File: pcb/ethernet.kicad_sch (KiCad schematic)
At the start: 46 parts, among them U9 W5500, Y1 25MHz

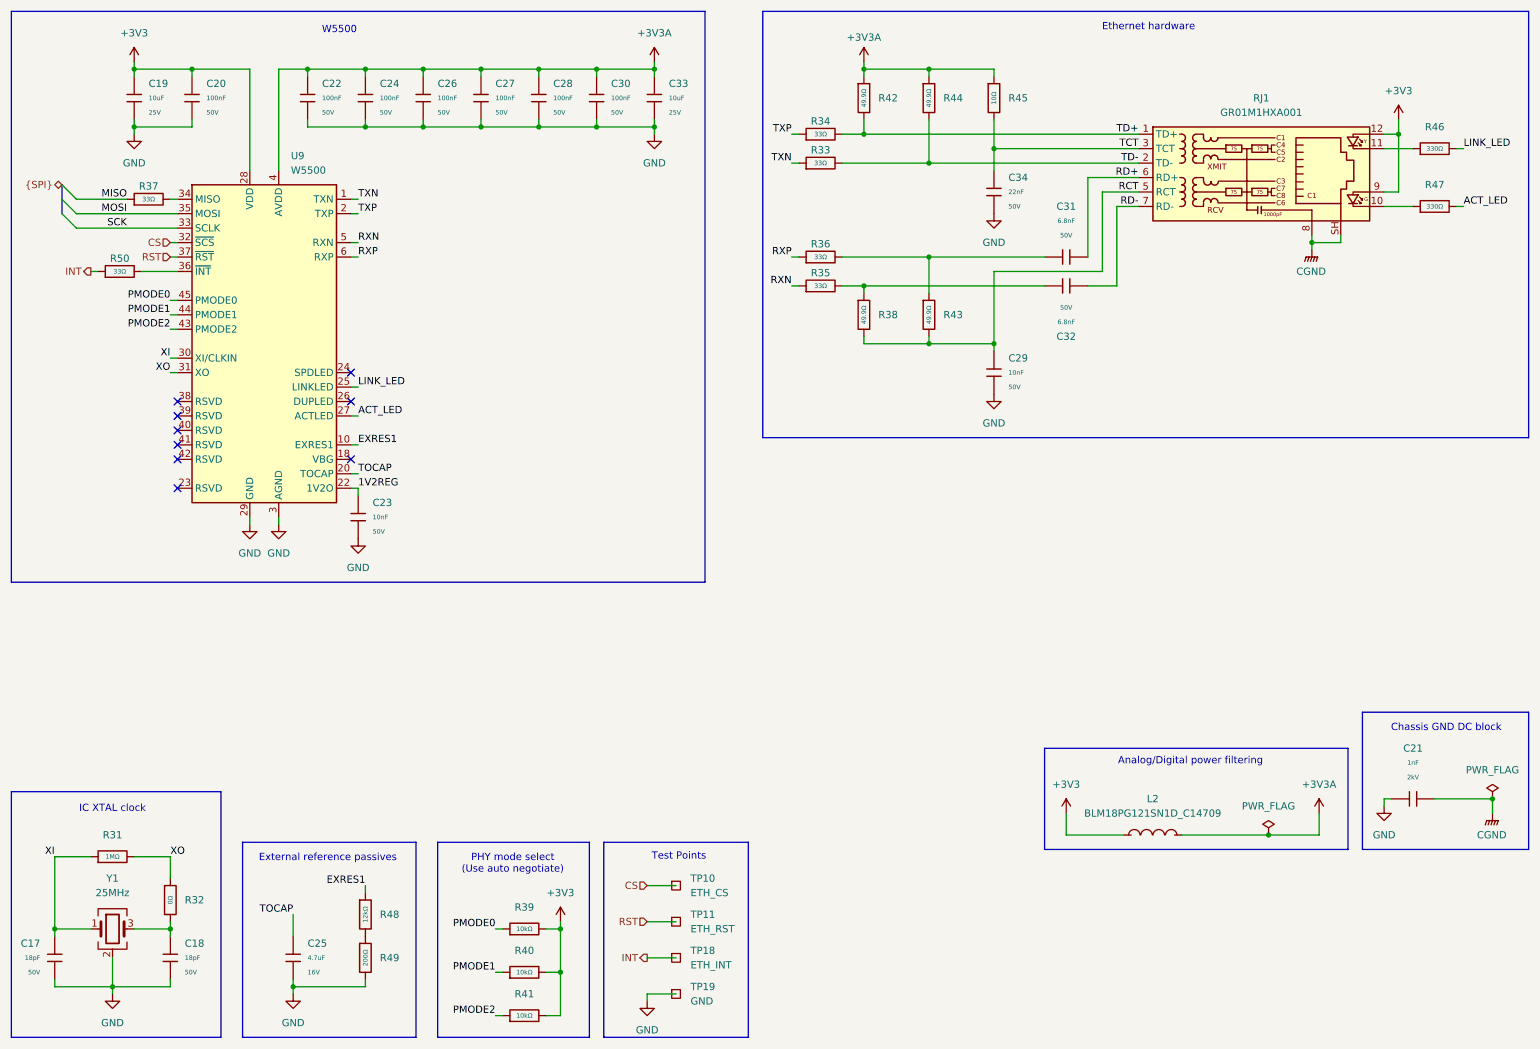
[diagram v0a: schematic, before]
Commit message: sch: rewire SPI to supply separate clock lines to flash and ethernet
The flash IC datasheet specifies that the SPI clock must not be toggled
while CS is high, which means we need to separate the ethernet and flash
clock lines.

I've GPIO3 on the ESP for the flash clock line, and plan to use the
internal peripheral MUX to switch it when talking with the IC.

I've also moved a bunch of test points and termination resistors in this
process.
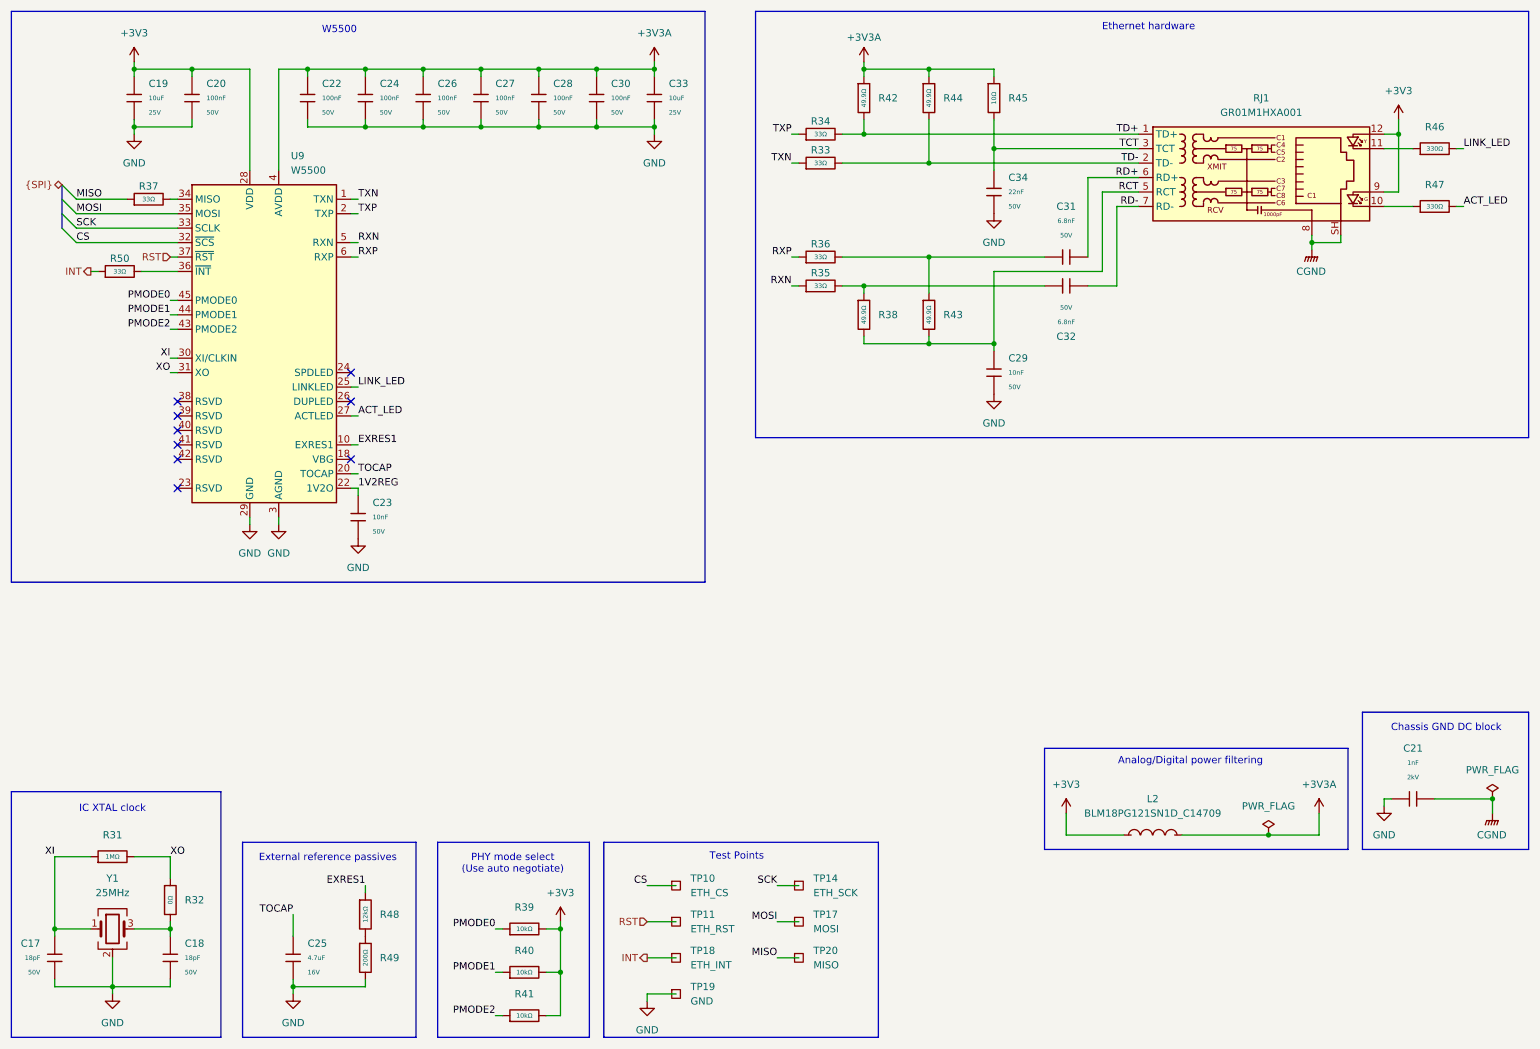
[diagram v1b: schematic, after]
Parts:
- added TP14: ETH_SCK, TestPoint:TestPoint_Pad_D1.0mm, symbol Connector:TestPoint_Square
- added TP17: MOSI, TestPoint:TestPoint_Pad_D1.0mm, symbol Connector:TestPoint_Square
- added TP20: MISO, TestPoint:TestPoint_Pad_D1.0mm, symbol Connector:TestPoint_Square
- TP10, TP11, TP18, TP19: now left out of the parts list
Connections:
- net MISO: now also TP20.1
- net MOSI: now also TP17.1
- net SCK: now also TP14.1

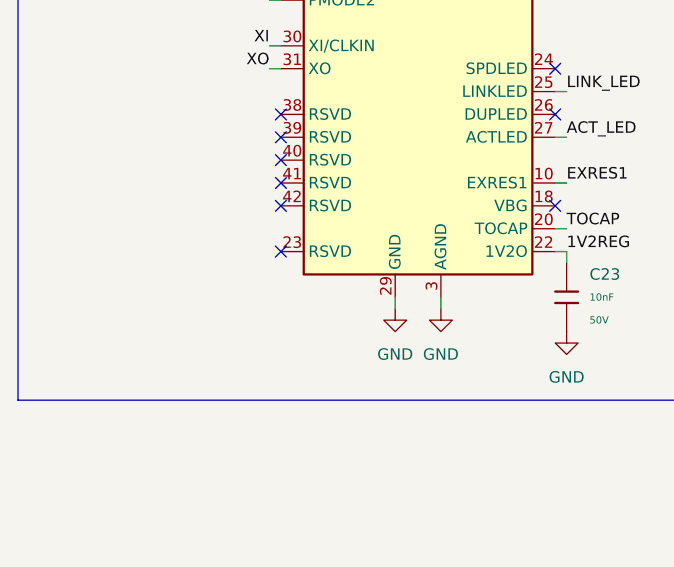
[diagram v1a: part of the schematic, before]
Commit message: sch: connect reserved W5500 pin 23 to ground
Pin 23 should be tied to ground according to the datasheet.
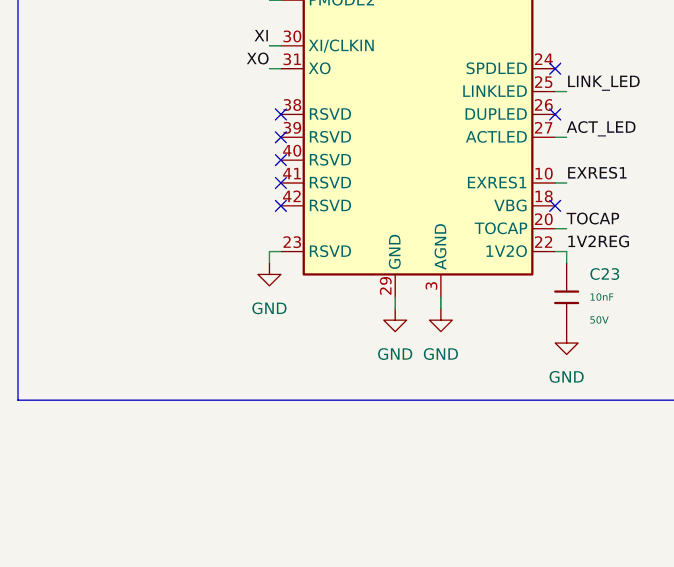
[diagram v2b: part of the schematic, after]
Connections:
- net GND: now also U9.23 (RSVD)
- no-connect marks 9 -> 8
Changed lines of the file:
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@@
 	)
 	(no_connect
-		(at 44.45 99.06)
-	)
-	(no_connect
 		(at 74.93 83.82)
 	)
@@
 	(wire
 		(pts
+			(xy 43.18 100.33) (xy 43.18 99.06)
+		)
+		(stroke
+			(width 0)
+			(type default)
+		)
+	)
+	(wire
+		(pts
 			(xy 176.53 25.4) (xy 187.96 25.4)
 		)
@@
 	(wire
 		(pts
+			(xy 43.18 99.06) (xy 44.45 99.06)
+		)
+		(stroke
+			(width 0)
+			(type default)
+		)
+	)
+	(wire
+		(pts
 			(xy 77.47 35.56) (xy 87.63 35.56)
 		)
@@
 					(unit 1)
 				)
+			)
+		)
+	)
+	(symbol
+		(lib_id "power:GND")
+		(at 43.18 100.33 0)
+		(mirror y)
+		(unit 1)
+		(body_style 1)
+		(exclude_from_sim no)
+		(in_bom yes)
+		(on_board yes)
+		(in_pos_files yes)
+		(dnp no)
+		(fields_autoplaced yes)
+		(property "Reference" "#PWR076"
+			(at 43.18 106.68 0)
+			(hide yes)
+			(show_name no)
+			(do_not_autoplace no)
+			(effects
+				(font
+					(size 1.27 1.27)
+				)
+			)
+		)
+		(property "Value" "GND"
+			(at 43.18 105.41 0)
+			(show_name no)
+			(do_not_autoplace no)
+			(effects
+				(font
+					(size 1.27 1.27)
+				)
+			)
+		)
+		(property "Footprint" ""
+			(at 43.18 100.33 0)
+			(hide yes)
+			(show_name no)
+			(do_not_autoplace no)
+			(effects
+				(font
+					(size 1.27 1.27)
+				)
+			)
+		)
+		(property "Datasheet" ""
+			(at 43.18 100.33 0)
+			(hide yes)
+			(show_name no)
+			(do_not_autoplace no)
+			(effects
+				(font
+					(size 1.27 1.27)
+				)
+			)
+		)
+		(property "Description" "Power symbol creates a global label with name \"GND\" , ground"
+			(at 43.18 100.33 0)
+			(hide yes)
+			(show_name no)
+			(do_not_autoplace no)
+			(effects
+				(font
+					(size 1.27 1.27)
+				)
+			)
+		)
+		(pin "1"
+		)
+		(instances
+			(project "EveningStar"
+				(path "/4c61f5a2-f8d4-462a-9bc3-d74437d30372/561d5dbe-6020-48c7-be42-1a6149a1119b"
+					(reference "#PWR076")
+					(unit 1)
+				)

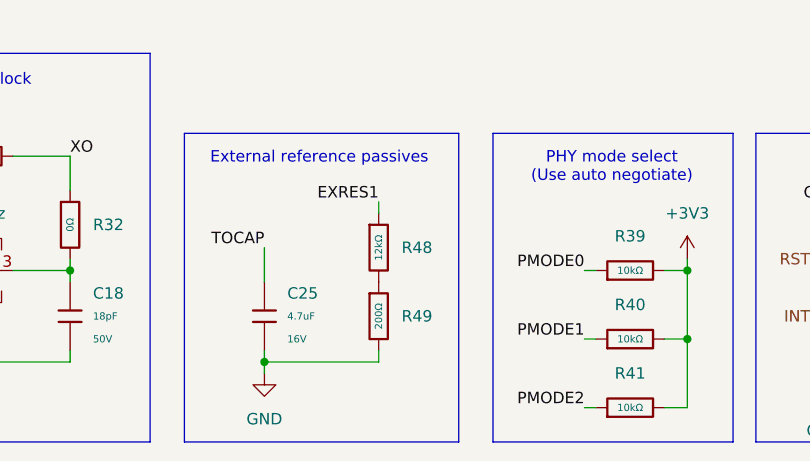
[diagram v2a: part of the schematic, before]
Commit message: sch: replace 12.2k w5500 exres with 12.4k
Datasheet specifies 12.4k resistor not 12.2k which was a mistake
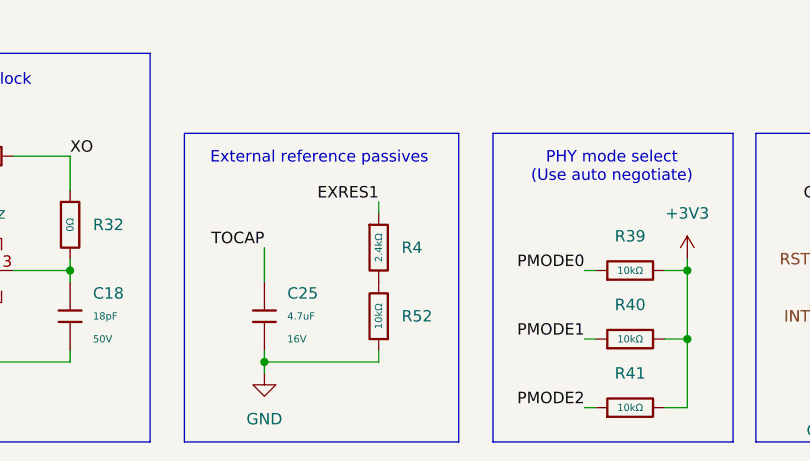
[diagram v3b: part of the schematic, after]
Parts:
- removed R48: 12kΩ, PCM_JLCPCB:R_0603, symbol PCM_JLCPCB-Resistors:0603,12kΩ
- removed R49: 200Ω, PCM_JLCPCB:R_0603, symbol PCM_JLCPCB-Resistors:0603,200Ω
- added R4: 2.4kΩ, PCM_JLCPCB:R_0603, symbol PCM_JLCPCB-Resistors:0603,2.4kΩ
- added R52: 10kΩ, PCM_JLCPCB:R_0603, symbol PCM_JLCPCB-Resistors:0603,10kΩ
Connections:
- net EXRES1: now also R4.1
- net GND: now also R52.1
- new net: R4.2, R52.2

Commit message: sch: add 3V3A ethernet TP
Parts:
- added TP35: +3V3A, TestPoint:TestPoint_Pad_D1.0mm, symbol Connector:TestPoint_Square
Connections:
- net +3V3A: now also TP35.1

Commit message: pcb(eth): layout w5500
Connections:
- net CGND: now also RJ1.13, RJ1.14; no longer RJ1.SH
- net RDMID-: now reaches C32.1, R35.2, R38.1
- net RDMID+: now reaches C31.1, R36.2, R43.1
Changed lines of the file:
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@@
 	)
 	(junction
+		(at 248.92 55.88)
+		(diameter 0)
+		(color 0 0 0 0)
+	)
+	(junction
 		(at 243.84 55.88)
 		(diameter 0)
@@
 	(wire
 		(pts
+			(xy 251.46 55.88) (xy 251.46 54.61)
+		)
+		(stroke
+			(width 0)
+			(type default)
+		)
+	)
+	(wire
+		(pts
 			(xy 36.83 26.67) (xy 36.83 25.4)
 		)
@@
 	(wire
 		(pts
+			(xy 248.92 55.88) (xy 251.46 55.88)
+		)
+		(stroke
+			(width 0)
+			(type default)
+		)
+	)
+	(wire
+		(pts
 			(xy 149.86 168.91) (xy 153.67 168.91)
 		)
@@
 		)
 	)
+	(label "RDMID+"
+		(at 165.1 58.42 0)
+		(effects
+			(font
+				(size 1.27 1.27)
+			)
+			(justify left bottom)
+		)
+	)
 	(label "TOCAP"
 		(at 76.2 96.52 0)
@@
 		)
 	)
+	(label "RDMID-"
+		(at 165.1 63.5 0)
+		(effects
+			(font
+				(size 1.27 1.27)
+			)
+			(justify left bottom)
+		)
+	)
 	(label "PMODE0"
 		(at 100.33 176.53 180)
@@
 		(pin "6"
 		)
-		(pin "SH"
+		(pin "14"
 		)
 		(pin "7"
@@
 		(pin "8"
 		)
+		(pin "13"
+		)
 		(instances

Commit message: pcb(eth): fix some drc errors
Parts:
- TP10, TP11, TP14, TP17, TP18, TP20, TP35: footprint TestPoint:TestPoint_Pad_D1.0mm -> custom:TestPoint_Pad_D1.0mm
- TP19: footprint TestPoint:TestPoint_Plated_Hole_D2.0mm -> custom:TestPoint_Plated_Hole_D2.0mm
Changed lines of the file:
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@@
 			)
 		)
-		(property "Footprint" "TestPoint:TestPoint_Pad_D1.0mm"
+		(property "Footprint" "custom:TestPoint_Pad_D1.0mm"
 			(at 137.16 181.61 0)
 			(hide yes)
@@
 			)
 		)
-		(property "Footprint" "TestPoint:TestPoint_Pad_D1.0mm"
+		(property "Footprint" "custom:TestPoint_Pad_D1.0mm"
 			(at 158.75 191.77 0)
 			(hide yes)
@@
 			)
 		)
-		(property "Footprint" "TestPoint:TestPoint_Pad_D1.0mm"
+		(property "Footprint" "custom:TestPoint_Pad_D1.0mm"
 			(at 158.75 175.26 0)
 			(hide yes)
@@
 			)
 		)
-		(property "Footprint" "TestPoint:TestPoint_Pad_D1.0mm"
+		(property "Footprint" "custom:TestPoint_Pad_D1.0mm"
 			(at 158.75 168.91 0)
 			(hide yes)
@@
 			)
 		)
-		(property "Footprint" "TestPoint:TestPoint_Plated_Hole_D2.0mm"
+		(property "Footprint" "custom:TestPoint_Plated_Hole_D2.0mm"
 			(at 137.16 187.96 0)
 			(hide yes)
@@
 			)
 		)
-		(property "Footprint" "TestPoint:TestPoint_Pad_D1.0mm"
+		(property "Footprint" "custom:TestPoint_Pad_D1.0mm"
 			(at 137.16 168.91 0)
 			(hide yes)
@@
 			)
 		)
-		(property "Footprint" "TestPoint:TestPoint_Pad_D1.0mm"
+		(property "Footprint" "custom:TestPoint_Pad_D1.0mm"
 			(at 158.75 181.61 0)
 			(hide yes)
@@
 			)
 		)
-		(property "Footprint" "TestPoint:TestPoint_Pad_D1.0mm"
+		(property "Footprint" "custom:TestPoint_Pad_D1.0mm"
 			(at 137.16 175.26 0)
 			(hide yes)

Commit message: pcb(footprints): fix footprint locality
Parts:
- U9: footprint Package_QFP:LQFP-48_7x7mm_P0.5mm -> custom:LQFP-48_7x7mm_P0.5mm
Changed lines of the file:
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@@
 			)
 		)
-		(property "Footprint" "Package_QFP:LQFP-48_7x7mm_P0.5mm"
+		(property "Footprint" "custom:LQFP-48_7x7mm_P0.5mm"
 			(at 59.69 31.75 0)
 			(hide yes)
